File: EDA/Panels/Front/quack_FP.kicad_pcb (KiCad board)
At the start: 2 copper layers, 60 x 22.8 mm, 4 parts

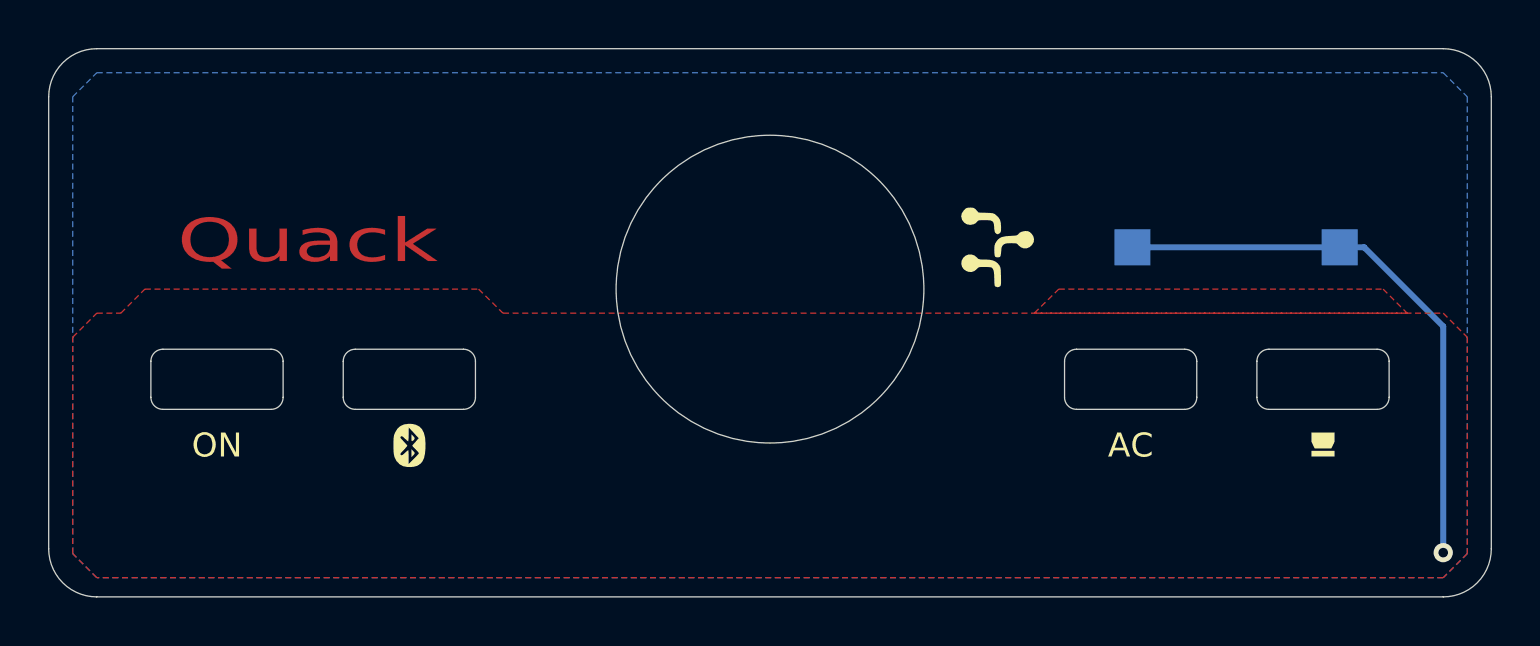
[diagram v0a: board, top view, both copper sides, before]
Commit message: New FR-4 based front panel with shine-through LEDs
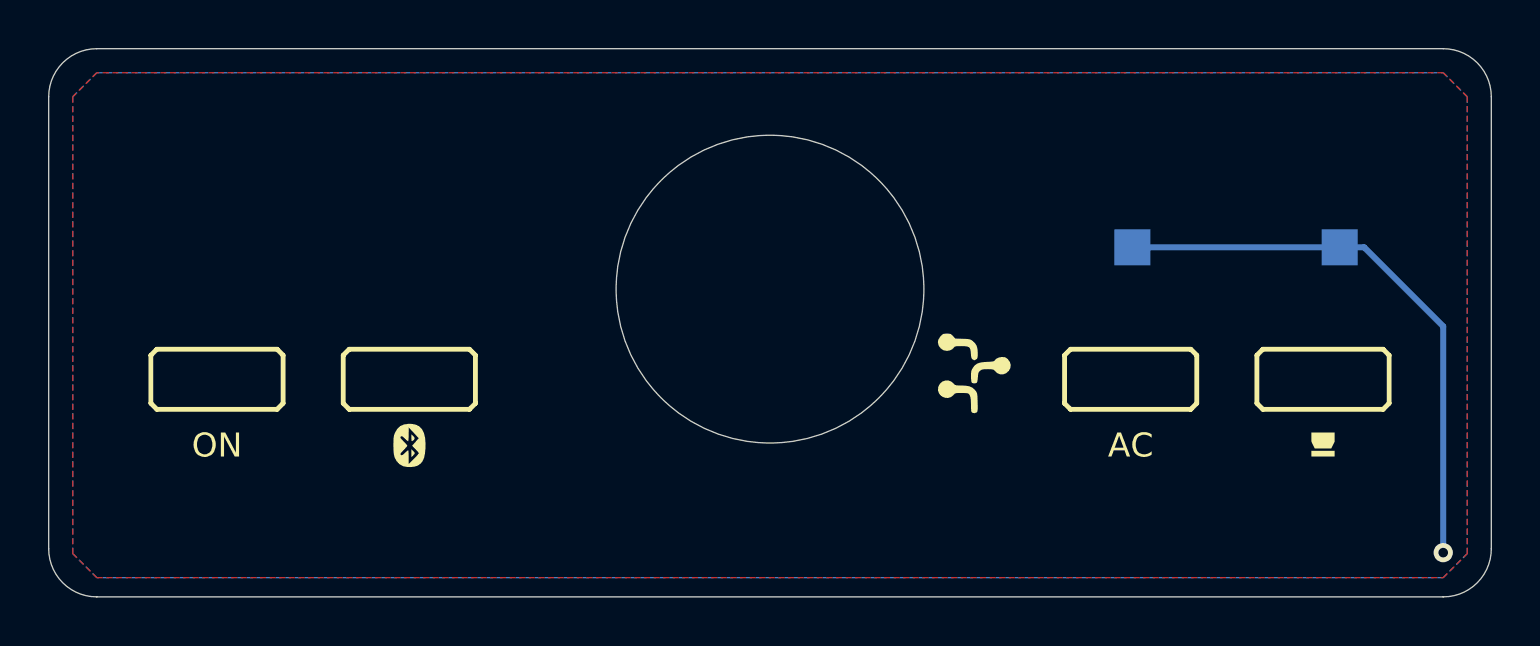
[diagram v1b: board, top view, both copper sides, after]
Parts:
- moved ADB 5.33 mm to (76.5, 53.5)
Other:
- outline, holes or cut-outs redrawn
- board text added: "Q"
- board text added: "Quack FR-4 front panel https://github.com/demik/quack"
- board text removed: "Quack"
